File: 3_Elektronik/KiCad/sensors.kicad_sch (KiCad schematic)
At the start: 26 parts, among them J6 693072010801, Q1 2N7002K, U1 LSM6DSV320XTR, U3 TCAN334, U5 LSM6DSO32XTR, U6 DPS310, U7 LIS3MDL

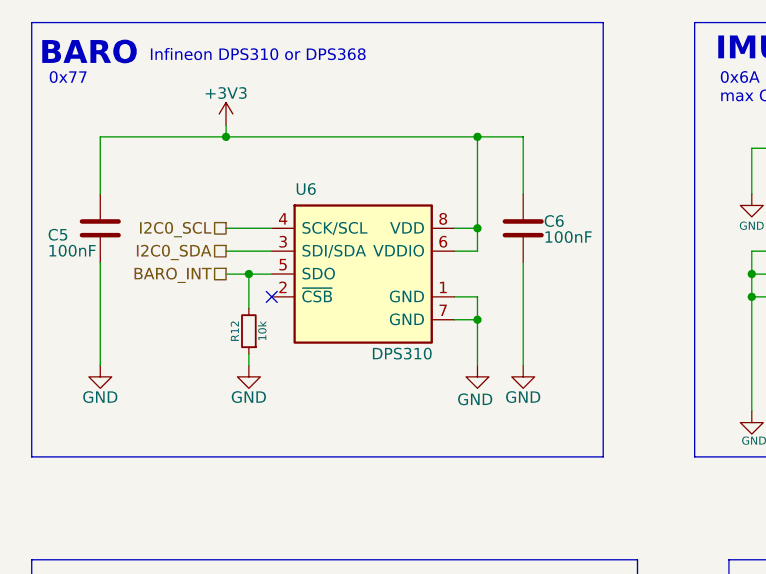
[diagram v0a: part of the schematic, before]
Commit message: build: :wrench: swap baro with meas ms5607
Use the MS5607 since it can measure up to ~30km above sea level.
The DPS was only able to measure up to ~9km.
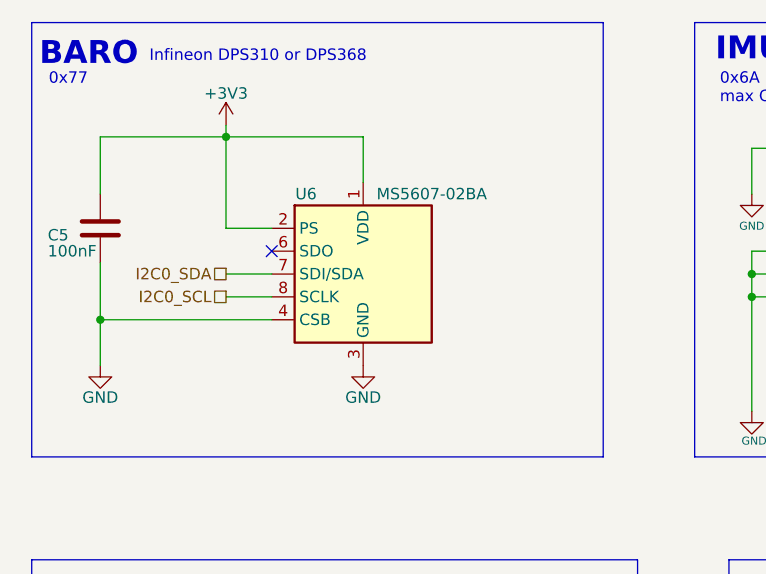
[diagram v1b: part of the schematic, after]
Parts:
- removed C6: 100nF, Capacitor_SMD:C_0603_1608Metric, symbol Device:C
- removed R12: 10k, Resistor_SMD:R_0603_1608Metric, symbol Device:R_Small
- U6: value DPS310 -> MS5607-02BA; footprint AUXSPACE:DPS310 -> AUXSPACE:MS5607-02BA03; symbol AUXSPACE:DPS310 -> Sensor_Pressure:MS5607-02BA; LCSC_PTNBR C130156 -> (none)
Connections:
- net BARO_INT is gone; now on net GND: U6.5 (CSB)
- net +3V3: now also U6.1 (VDD), U6.2 (PS); no longer U6.6 (VDDIO), U6.8 (VDD)
- net GND: now also U6.3 (GND), U6.4 (CSB); no longer U6.1 (GND), U6.7 (GND)
- net I2C0_SCL: now also U6.8 (SCLK); no longer U6.4 (SCK/SCL)
- net I2C0_SDA: now also U6.7 (SDI/SDA); no longer U6.3 (SDI/SDA)
